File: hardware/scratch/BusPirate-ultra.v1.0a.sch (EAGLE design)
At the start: 133 parts, among them IC1 IC_MEM_23LC1024, IC10 IC_BUFF_SN74LVC1T45DBV, IC11 IC_BUFF_SN74LVC1T45DBV, IC12 74LVC1G07DBV, IC13 IC_BUFF_SN74LVC1T45DBV, IC14 IC_BL1551, IC15 IC_BL1551, IC16 74HCT4066PW, IC2 IC_MEM_23LC1024, IC3 IC_74AC573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

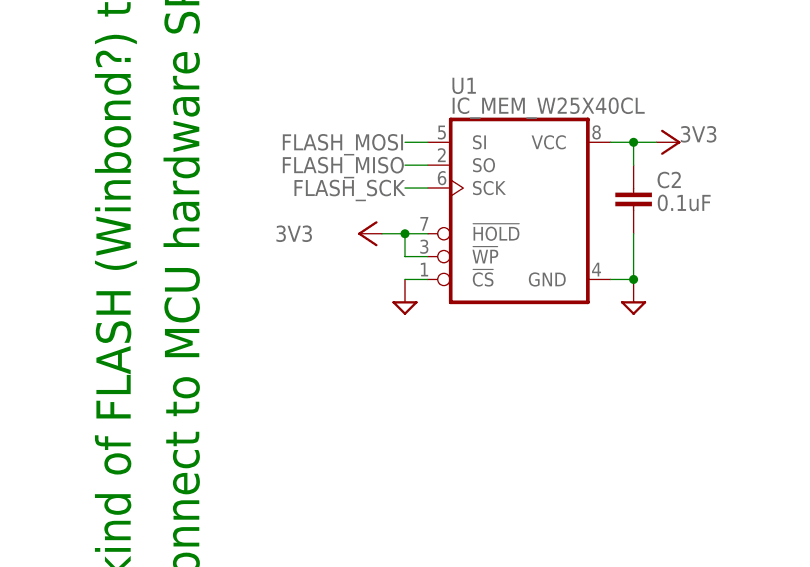
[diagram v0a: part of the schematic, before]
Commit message: increment version to Bus Pirate Ultra v1.0a, removed previous BusPirate-ng.v4.0 files flash CS pin wired to GND fix ARM and FPGA chip pin 1 indicator fix bl1331 pin 1
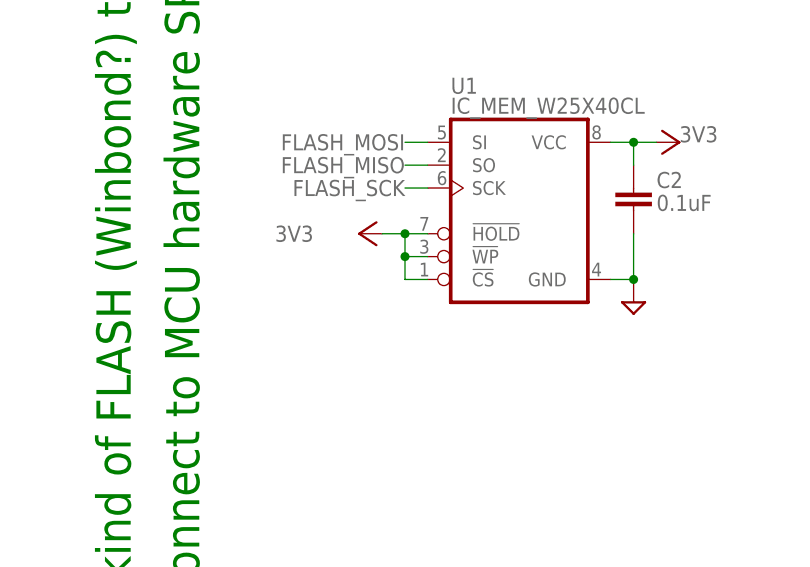
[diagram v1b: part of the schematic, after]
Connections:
- net 3V3: now also U1.!CS
- net GND: no longer U1.!CS
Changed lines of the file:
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@@
 <part name="CONN1" library="dp_devices.v6" deviceset="CON-USB-F-MICRO-B-2" device=""/>
 <part name="U1" library="dp_devices.v6" deviceset="IC_MEM_W25X40CL" device=""/>
-<part name="SUPPLY100" library="supply2" deviceset="GND" device=""/>
 <part name="SUPPLY101" library="supply2" deviceset="GND" device=""/>
 <part name="+3V1" library="dp_devices.v6" deviceset="SUPPLY_+3V3" device=""/>
@@
 <instance part="CONN1" gate="BGND" x="-350.52" y="452.12"/>
 <instance part="U1" gate="U" x="-264.16" y="335.28"/>
-<instance part="SUPPLY100" gate="GND" x="-276.86" y="325.12" smashed="yes"/>
 <instance part="SUPPLY101" gate="GND" x="-251.46" y="325.12" smashed="yes"/>
 <instance part="+3V1" gate="G$1" x="-279.4" y="332.74" smashed="yes" rot="R90"/>
@@
 <pinref part="C48" gate="G$1" pin="1"/>
 <pinref part="SUPPLY83" gate="GND" pin="GND"/>
-</segment>
-<segment>
-<pinref part="U1" gate="U" pin="!CS"/>
-<pinref part="SUPPLY100" gate="GND" pin="GND"/>
-<wire x1="-274.32" y1="327.66" x2="-276.86" y2="327.66" width="0.1524" layer="91"/>
 </segment>
 <segment>
@@
 <junction x="-276.86" y="332.74"/>
 <label x="-287.02" y="332.74" size="1.778" layer="95" align="center-right"/>
-</segment>
-<segment>
+<pinref part="U1" gate="U" pin="!CS"/>
+<wire x1="-274.32" y1="327.66" x2="-276.86" y2="327.66" width="0.1524" layer="91"/>
+<wire x1="-276.86" y1="327.66" x2="-276.86" y2="330.2" width="0.1524" layer="91"/>
+<junction x="-276.86" y="330.2"/>
+</segment>
+<segment>

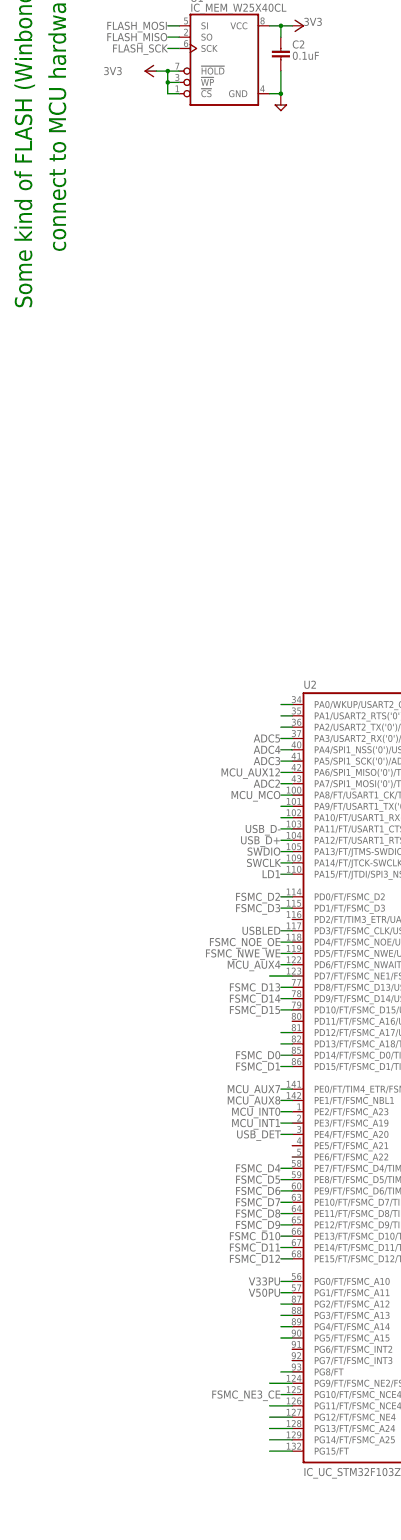
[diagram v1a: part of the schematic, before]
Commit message: flash CS now connected to STM's PG15
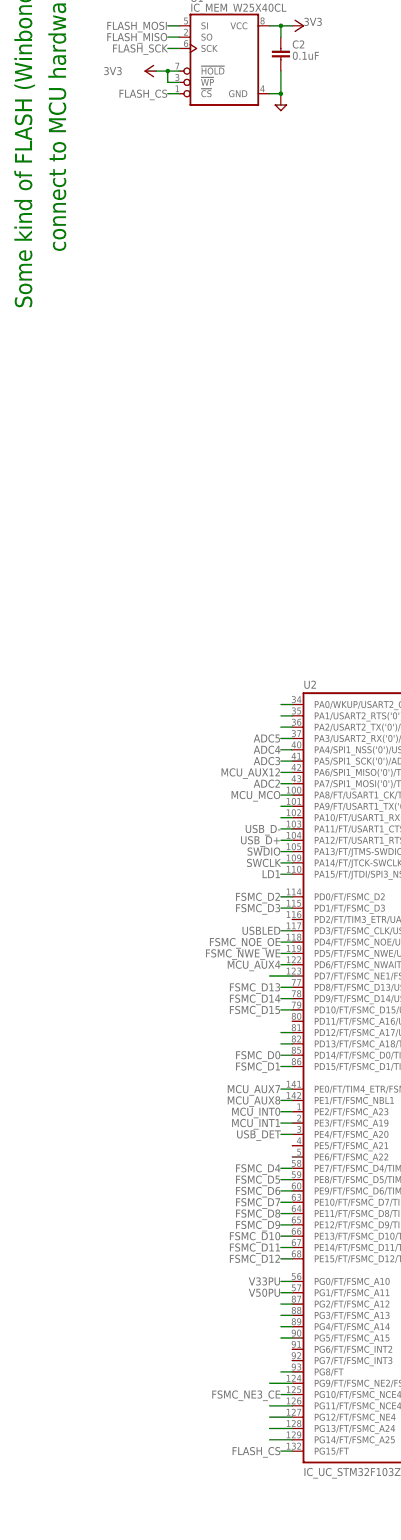
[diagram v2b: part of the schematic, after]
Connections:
- removed net N$61: U2U.PG15/FT
- new net FLASH_CS: U1.!CS, U2U.PG15/FT
- net 3V3: no longer U1.!CS
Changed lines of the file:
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@@
 <junction x="-276.86" y="332.74"/>
 <label x="-287.02" y="332.74" size="1.778" layer="95" align="center-right"/>
-<pinref part="U1" gate="U" pin="!CS"/>
-<wire x1="-274.32" y1="327.66" x2="-276.86" y2="327.66" width="0.1524" layer="91"/>
-<wire x1="-276.86" y1="327.66" x2="-276.86" y2="330.2" width="0.1524" layer="91"/>
-<junction x="-276.86" y="330.2"/>
 </segment>
 <segment>
@@
 </segment>
 </net>
-<net name="N$61" class="0">
-<segment>
-<pinref part="U2" gate="U" pin="PG15/FT"/>
-<wire x1="-248.92" y1="22.86" x2="-254" y2="22.86" width="0.1524" layer="91"/>
-</segment>
-</net>
 <net name="MCU_AUX2" class="0">
 <segment>
@@
 </segment>
 </net>
+<net name="FLASH_CS" class="0">
+<segment>
+<pinref part="U1" gate="U" pin="!CS"/>
+<wire x1="-274.32" y1="327.66" x2="-276.86" y2="327.66" width="0.1524" layer="91"/>
+<label x="-276.86" y="327.66" size="1.778" layer="95" align="center-right"/>
+</segment>
+<segment>
+<pinref part="U2" gate="U" pin="PG15/FT"/>
+<wire x1="-248.92" y1="22.86" x2="-251.46" y2="22.86" width="0.1524" layer="91"/>
+<label x="-251.46" y="22.86" size="1.778" layer="95" align="center-right"/>
+</segment>
+</net>
